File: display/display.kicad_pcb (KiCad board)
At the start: 2 copper layers, 68.4 x 20.5 mm, 46 parts, among them P1 CONN_14

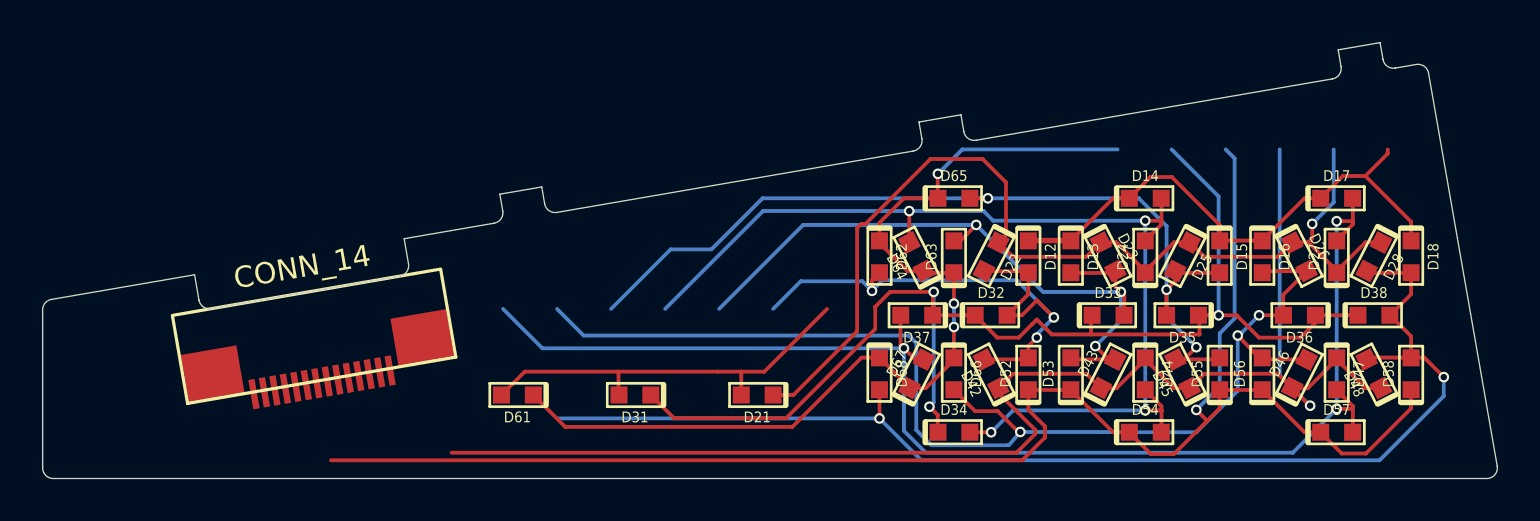
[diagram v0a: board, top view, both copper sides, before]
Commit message: Loosely place column wires near the connector.
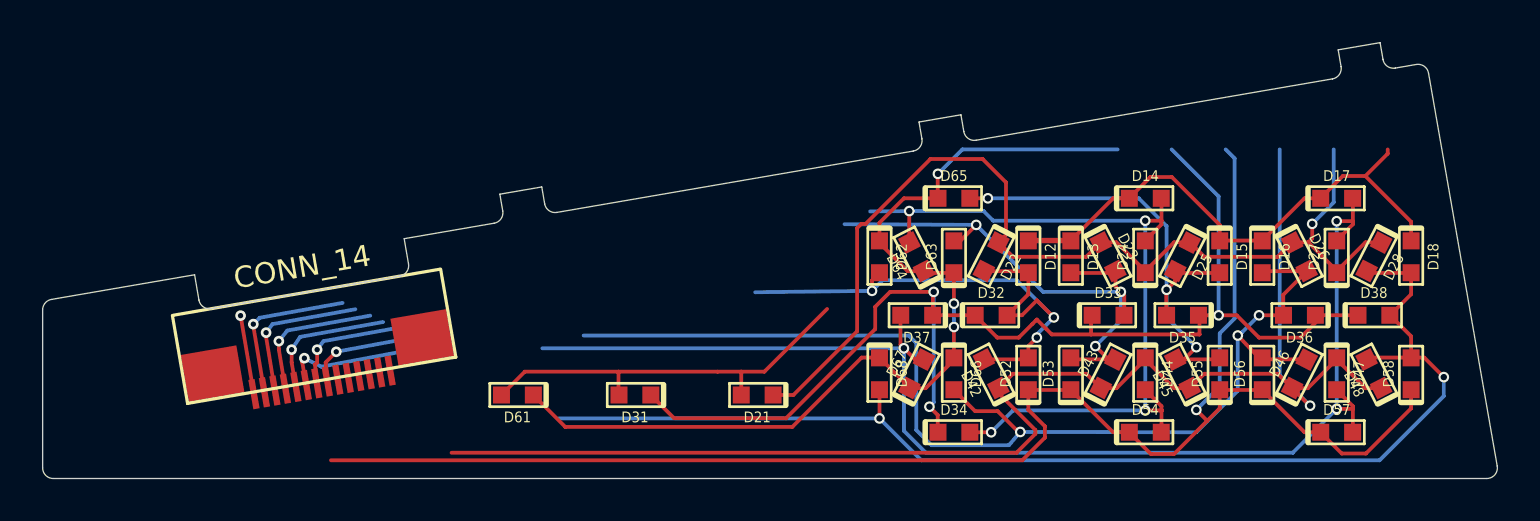
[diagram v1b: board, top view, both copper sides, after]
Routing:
- net (no net): track 667.5 -> 624.2 mm
- net /COL7: track 0.00 -> 7.64 mm, vias 0 -> 1
- net /COL6: track 0.00 -> 7.22 mm, vias 0 -> 1
- net /COL3: track 0.00 -> 7.08 mm, vias 0 -> 1
- net /COL5: track 0.00 -> 6.86 mm, vias 0 -> 1
- net /COL4: track 0.00 -> 6.45 mm, vias 0 -> 1
- net /COL2: track 0.00 -> 6.09 mm, vias 0 -> 1
- net /COL1: track 0.00 -> 5.98 mm, vias 0 -> 1
- net /COL8: track 0.00 -> 3.74 mm, vias 0 -> 1
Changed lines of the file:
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@@
     (thickness 1.6002)
     (drawings 33)
-    (tracks 348)
+    (tracks 375)
     (zones 0)
     (modules 46)
@@
   (gr_line (start 135.992156 96.388669) (end 136.127883 97.177067) (angle 90) (layer Edge.Cuts) (width 0.01))
   (gr_arc (start 135.635143 97.2619) (end 135.719962 97.754651) (angle -90.01309679) (layer Edge.Cuts) (width 0.01))
+  (segment (start 155.24226 97.18294) (end 153.4 97.2) (width 0.1778) (layer Back) (net 0))
+  (segment (start 158.10484 96.5835) (end 158.9405 96.5835) (width 0.1778) (layer Front) (net 0))
+  (via (at 158.9405 96.5835) (size 0.50038) (drill 0.29972) (layers Front Back) (net 0))
+  (segment (start 158.9405 96.5835) (end 166.04234 96.5835) (width 0.1778) (layer Back) (net 0))
+  (segment (start 166.04234 96.5835) (end 167.34282 97.88398) (width 0.1778) (layer Back) (net 0))
+  (segment (start 167.34282 97.88398) (end 167.34282 100.88372) (width 0.1778) (layer Back) (net 0))
+  (segment (start 158.39186 97.83318) (end 152.2 97.8) (width 0.1778) (layer Back) (net 0))
+  (segment (start 153.4922 100.93452) (end 148 101) (width 0.1778) (layer Back) (net 0))
   (segment (start 149.74316 107.33278) (end 139.06886 107.33278) (width 0.1778) (layer Front) (net 0))
   (segment (start 156.58084 95.44304) (end 156.58084 96.5835) (width 0.1778) (layer Front) (net 0))
@@
   (via (at 157.34284 101.53396) (size 0.50038) (drill 0.29972) (layers Front Back) (net 0))
   (segment (start 165.04158 94.2848) (end 157.73908 94.2848) (width 0.1778) (layer Back) (net 0))
-  (segment (start 139.06886 107.33278) (end 137.56772 105.83164) (width 0.1778) (layer Front) (net 0) (status 800000))
+  (segment (start 139.06886 107.33278) (end 137.56772 105.83164) (width 0.1778) (layer Front) (net 0))
   (segment (start 141.57 104.73436) (end 137.165 104.73436) (width 0.1778) (layer Front) (net 0))
   (segment (start 137.165 104.73436) (end 136.06772 105.83164) (width 0.1778) (layer Front) (net 0))
@@
   (via (at 161.24174 103.13416) (size 0.50038) (drill 0.29972) (layers Front Back) (net 0))
   (segment (start 161.24174 102.9843) (end 161.24174 103.13416) (width 0.1778) (layer Back) (net 0))
-  (segment (start 153.4922 100.93452) (end 153.04262 100.48494) (width 0.1778) (layer Back) (net 0))
-  (segment (start 150.14194 100.48494) (end 148.84146 101.78542) (width 0.1778) (layer Back) (net 0))
-  (segment (start 153.04262 100.48494) (end 150.14194 100.48494) (width 0.1778) (layer Back) (net 0))
   (segment (start 160.29178 100.43414) (end 162.04184 102.1842) (width 0.1778) (layer Back) (net 0))
   (segment (start 153.99004 100.43414) (end 160.29178 100.43414) (width 0.1778) (layer Back) (net 0))
@@
   (segment (start 158.74492 100.00996) (end 160.75914 100.00996) (width 0.1778) (layer Front) (net 0))
   (segment (start 160.75914 100.00996) (end 160.84296 100.09378) (width 0.1778) (layer Front) (net 0))
-  (segment (start 158.39186 97.83318) (end 150.2537 97.83318) (width 0.1778) (layer Back) (net 0))
-  (segment (start 150.2537 97.83318) (end 146.30146 101.78542) (width 0.1778) (layer Back) (net 0))
   (segment (start 157.34284 98.56978) (end 157.65526 98.56978) (width 0.1778) (layer Front) (net 0))
   (segment (start 161.54146 100.98278) (end 165.19144 100.98278) (width 0.1778) (layer Back) (net 0))
@@
   (segment (start 162.84194 100.09378) (end 164.85616 100.09378) (width 0.1778) (layer Front) (net 0))
   (segment (start 164.85616 100.09378) (end 164.93998 100.00996) (width 0.1778) (layer Front) (net 0))
-  (segment (start 143.76146 101.78542) (end 148.36394 97.18294) (width 0.1778) (layer Back) (net 0))
-  (segment (start 148.36394 97.18294) (end 155.24226 97.18294) (width 0.1778) (layer Back) (net 0))
   (segment (start 166.33952 97.63506) (end 159.19196 97.63506) (width 0.1778) (layer Back) (net 0))
   (segment (start 155.24226 98.65106) (end 155.2448 98.6536) (width 0.1778) (layer Front) (net 0))
@@
   (segment (start 167.10406 97.63506) (end 167.10406 97.80778) (width 0.1778) (layer Front) (net 0))
   (segment (start 167.10406 97.80778) (end 166.34206 98.56978) (width 0.1778) (layer Front) (net 0))
-  (segment (start 141.22146 101.78542) (end 144.02308 98.9838) (width 0.1778) (layer Back) (net 0))
-  (segment (start 148.34362 96.5835) (end 158.9405 96.5835) (width 0.1778) (layer Back) (net 0))
-  (segment (start 145.94332 98.9838) (end 148.34362 96.5835) (width 0.1778) (layer Back) (net 0))
-  (segment (start 144.02308 98.9838) (end 145.94332 98.9838) (width 0.1778) (layer Back) (net 0))
-  (segment (start 158.10484 96.5835) (end 158.9405 96.5835) (width 0.1778) (layer Front) (net 0))
-  (segment (start 167.34282 97.88398) (end 167.34282 100.88372) (width 0.1778) (layer Back) (net 0))
-  (segment (start 166.04234 96.5835) (end 167.34282 97.88398) (width 0.1778) (layer Back) (net 0))
-  (segment (start 158.9405 96.5835) (end 166.04234 96.5835) (width 0.1778) (layer Back) (net 0))
-  (via (at 158.9405 96.5835) (size 0.50038) (drill 0.29972) (layers Front Back) (net 0))
   (segment (start 167.74414 100.00996) (end 167.74414 100.4824) (width 0.1778) (layer Front) (net 0))
   (segment (start 167.74414 100.4824) (end 167.34282 100.88372) (width 0.1778) (layer Front) (net 0))
@@
   (via (at 160.4645 107.569) (size 0.50038) (drill 0.29972) (layers Front Back) (net 0))
   (segment (start 160.4645 107.569) (end 159.9311 108.1913) (width 0.1778) (layer Back) (net 0))
-  (segment (start 139.93114 103.0351) (end 138.68146 101.78542) (width 0.1778) (layer Back) (net 0))
   (segment (start 155.2194 103.0351) (end 139.93114 103.0351) (width 0.1778) (layer Back) (net 0))
   (segment (start 155.575 103.3907) (end 155.2194 103.0351) (width 0.1778) (layer Back) (net 0))
@@
   (segment (start 173.2788 108.5469) (end 156.0195 108.5469) (width 0.1778) (layer Back) (net 0))
   (segment (start 154.9908 103.63454) (end 137.99058 103.63454) (width 0.1778) (layer Back) (net 0))
-  (segment (start 137.99058 103.63454) (end 136.14146 101.78542) (width 0.1778) (layer Back) (net 0))
   (segment (start 154.83078 102.0826) (end 154.83078 103.47452) (width 0.1778) (layer Front) (net 0) (status 10))
   (segment (start 154.83078 103.47452) (end 154.9908 103.63454) (width 0.1778) (layer Front) (net 0))
@@
   (segment (start 176.71542 108.585) (end 175.58258 108.585) (width 0.1778) (layer Front) (net 0))
   (segment (start 178.8414 106.45902) (end 176.71542 108.585) (width 0.1778) (layer Front) (net 0))
+  (segment (start 132.6 103) (end 128.3 103.8) (width 0.1778) (layer Back) (net 1))
+  (via (at 128.3 103.8) (size 0.50038) (layers Front Back) (net 1))
+  (segment (start 127.8 104.3) (end 127.878253 105.194702) (width 0.1778) (layer Front) (net 1))
+  (segment (start 128.3 103.8) (end 127.8 104.3) (width 0.1778) (layer Front) (net 1))
+  (segment (start 127.4 103.7) (end 127.7 103.3) (width 0.1778) (layer Back) (net 2))
+  (segment (start 127.4 104.3) (end 127.4 103.7) (width 0.1778) (layer Front) (net 2))
+  (via (at 127.4 103.7) (size 0.50038) (layers Front Back) (net 2))
+  (segment (start 127.385549 105.279806) (end 127.3 104.4) (width 0.1778) (layer Front) (net 2))
+  (segment (start 127.3 104.4) (end 127.4 104.3) (width 0.1778) (layer Front) (net 2))
+  (segment (start 127.7 103.3) (end 131.6 102.6) (width 0.1778) (layer Back) (net 2))
+  (segment (start 126.8 104.1) (end 127.6 104.5) (width 0.1778) (layer Back) (net 3))
+  (segment (start 126.892845 105.364911) (end 126.7 104.3) (width 0.1778) (layer Front) (net 3))
+  (via (at 126.8 104.1) (size 0.50038) (layers Front Back) (net 3))
+  (segment (start 126.7 104.3) (end 126.8 104.1) (width 0.1778) (layer Front) (net 3))
+  (segment (start 127.6 104.5) (end 132.4 103.6) (width 0.1778) (layer Back) (net 3))
+  (segment (start 126.2 103.7) (end 126.6 103.1) (width 0.1778) (layer Back) (net 4))
+  (segment (start 126.2 104.3) (end 126.2 103.7) (width 0.1778) (layer Front) (net 4))
+  (via (at 126.2 103.7) (size 0.50038) (layers Front Back) (net 4))
+  (segment (start 126.400141 105.450016) (end 126.2 104.3) (width 0.1778) (layer Front) (net 4))
+  (segment (start 126.6 103.1) (end 130.5 102.4) (width 0.1778) (layer Back) (net 4))
+  (segment (start 125.6 103.3) (end 126 102.8) (width 0.1778) (layer Back) (net 5))
+  (segment (start 125.6 103.7) (end 125.6 103.3) (width 0.1778) (layer Front) (net 5))
+  (via (at 125.6 103.3) (size 0.50038) (layers Front Back) (net 5))
+  (segment (start 125.907437 105.535121) (end 125.6 103.7) (width 0.1778) (layer Front) (net 5))
+  (segment (start 126 102.8) (end 129.9 102.1) (width 0.1778) (layer Back) (net 5))
+  (segment (start 125 102.9) (end 125.3 102.5) (width 0.1778) (layer Back) (net 6))
+  (segment (start 125 103.1) (end 125 102.9) (width 0.1778) (layer Front) (net 6))
+  (via (at 125 102.9) (size 0.50038) (layers Front Back) (net 6))
+  (segment (start 125.414733 105.620225) (end 125 103.1) (width 0.1778) (layer Front) (net 6))
+  (segment (start 125.3 102.5) (end 129.2 101.8) (width 0.1778) (layer Back) (net 6))
+  (segment (start 128.6 101.5) (end 124.7 102.2) (width 0.1778) (layer Back) (net 7))
+  (segment (start 124.4 102.6) (end 124.922029 105.70533) (width 0.1778) (layer Front) (net 7))
+  (via (at 124.4 102.5) (size 0.50038) (layers Front Back) (net 7))
+  (segment (start 124.4 102.6) (end 124.4 102.5) (width 0.1778) (layer Front) (net 7))
+  (segment (start 124.7 102.2) (end 124.4 102.5) (width 0.1778) (layer Back) (net 7))
+  (via (at 123.8 102.1) (size 0.50038) (layers Front Back) (net 8) (status 40000))
+  (segment (start 123.8 102.1) (end 124.429325 105.790435) (width 0.1778) (layer Front) (net 8) (status 40000))
 )

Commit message: Route almost every row and column.
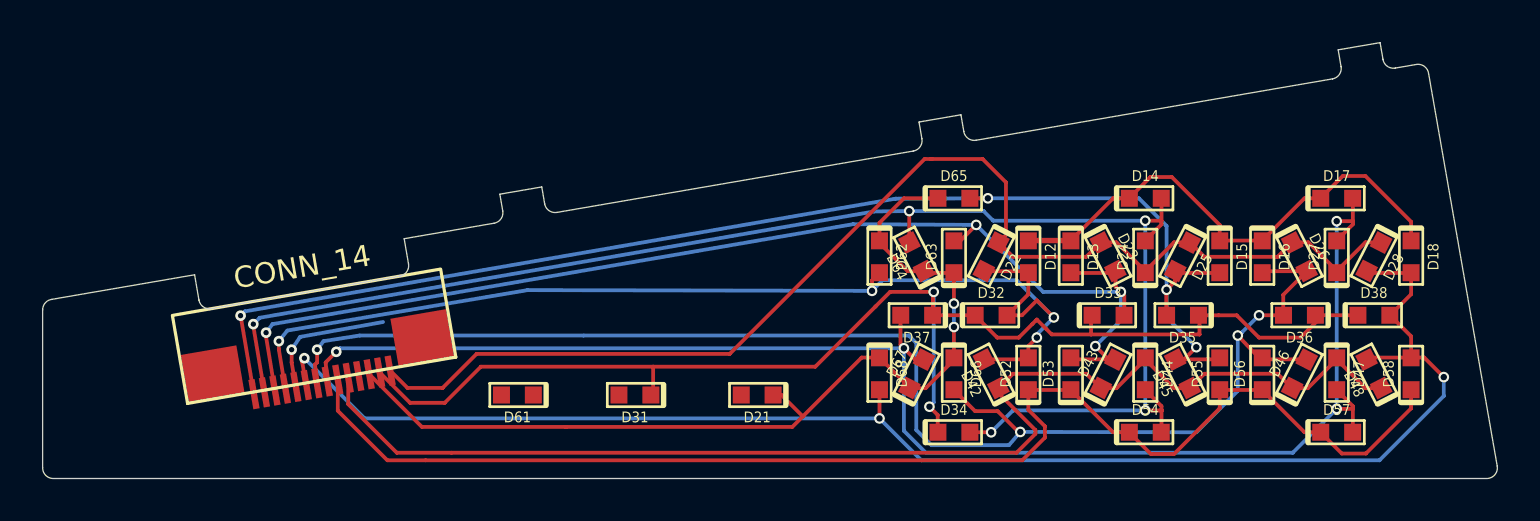
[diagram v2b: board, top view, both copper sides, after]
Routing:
- net (no net): track 624.2 -> 23.9 mm, vias 30 -> 0
- net /COL1: track 5.98 -> 71.6 mm, vias 1 -> 4
- net /COL3: track 7.08 -> 71.3 mm, vias 1 -> 3
- net /COL7: track 7.64 -> 71.1 mm, vias 1 -> 5
- net /ROW6: track 0.00 -> 62.7 mm
- net /ROW2: track 0.00 -> 62.3 mm, vias 0 -> 2
- net /COL2: track 6.09 -> 68.2 mm, vias 1 -> 4
- net /COL8: track 3.74 -> 63.2 mm, vias 1 -> 4
- net /ROW5: track 0.00 -> 59.4 mm
- net /ROW1: track 0.00 -> 59.0 mm
- net /COL6: track 7.22 -> 57.0 mm, vias 1 -> 4
- net /COL5: track 6.86 -> 52.9 mm, vias 1 -> 4
- net /ROW3: track 0.00 -> 45.2 mm, vias 0 -> 2

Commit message: Route every track.
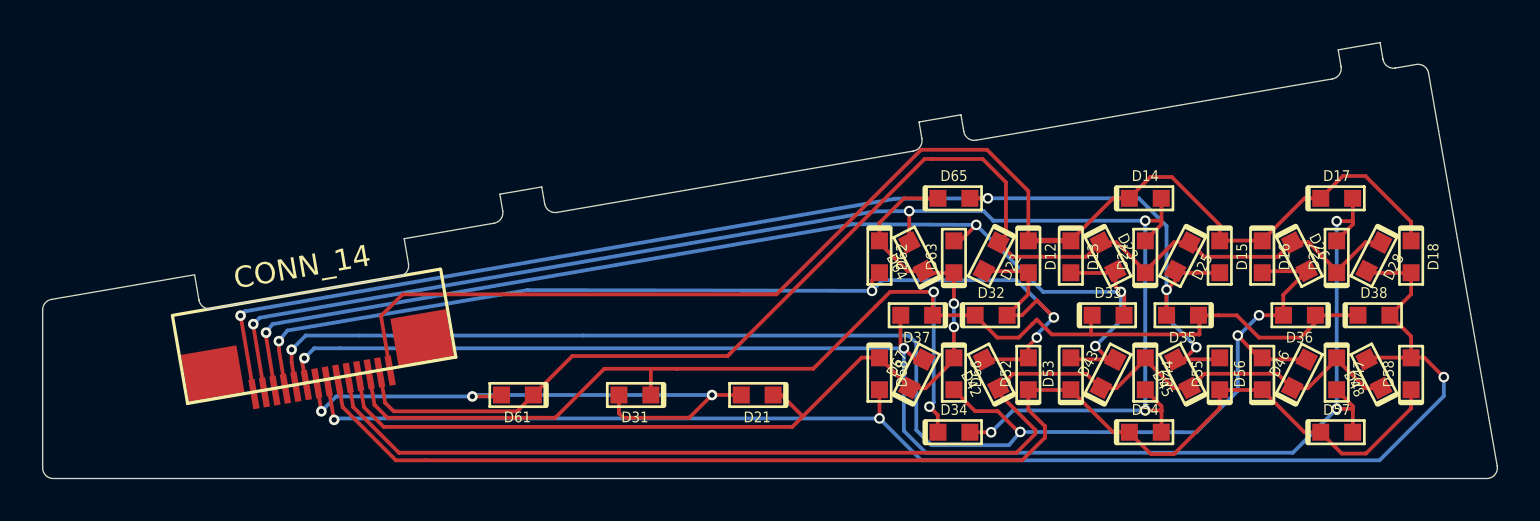
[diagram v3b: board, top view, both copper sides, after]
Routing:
- net /COL2: track 68.2 -> 1.34 mm, vias 4 -> 1
- net /COL4: track 6.45 -> 69.6 mm, vias 1 -> 4
- net /ROW4: track 0.00 -> 46.3 mm, vias 0 -> 2
- net /ROW3: track 45.2 -> 64.0 mm
- net /ROW1: track 59.0 -> 63.4 mm
- net (no net): track 23.9 -> 27.2 mm, vias 0 -> 2
- net /COL1: track 71.6 -> 69.3 mm, vias 4 -> 3
- net /COL3: track 71.3 -> 72.9 mm, vias 3 -> 4
- net /ROW2: track 62.3 -> 60.9 mm, vias 2 -> 0

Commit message: Make routing nicer by not using so many tracks that are not multiplies of 45 angles.
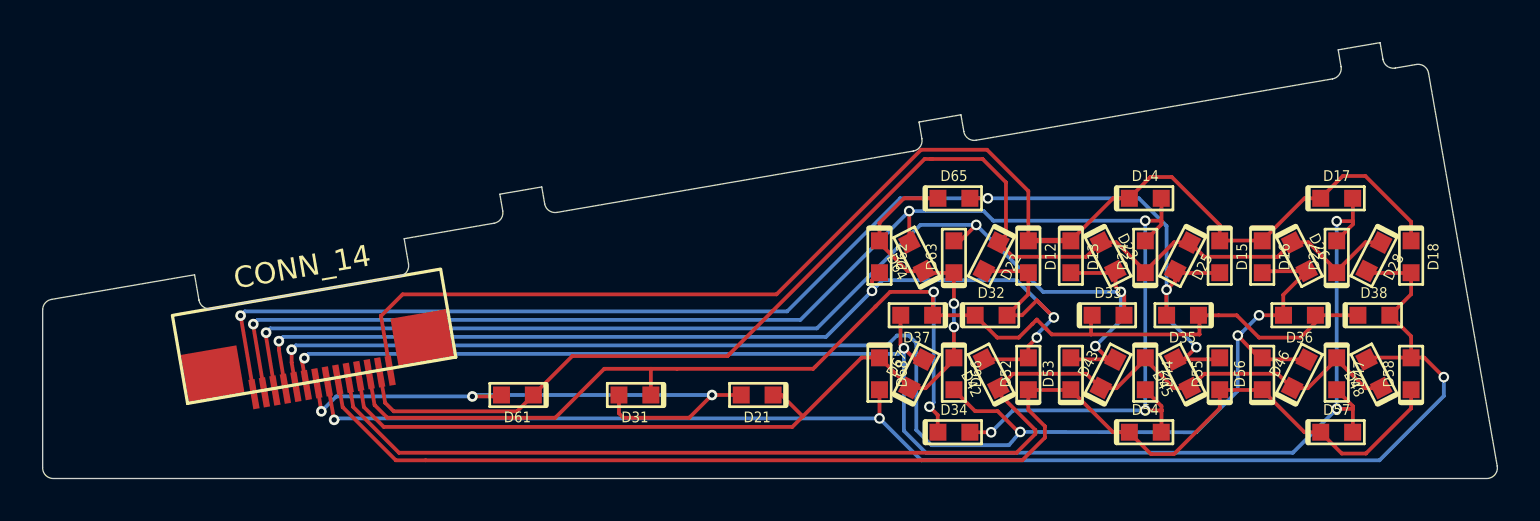
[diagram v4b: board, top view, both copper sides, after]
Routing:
- net /COL2: track 1.34 -> 28.6 mm, vias 1 -> 3
- net (no net): track 27.2 -> 0.00 mm, vias 2 -> 0
- net /COL8: track 63.2 -> 65.0 mm
- net /COL7: track 71.1 -> 72.8 mm
- net /COL6: track 57.0 -> 58.5 mm
- net /COL5: track 52.9 -> 53.5 mm
